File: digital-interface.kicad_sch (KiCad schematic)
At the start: 23 parts, among them U701 Si8641BD-B-IS2, U702 R05C05TE05S

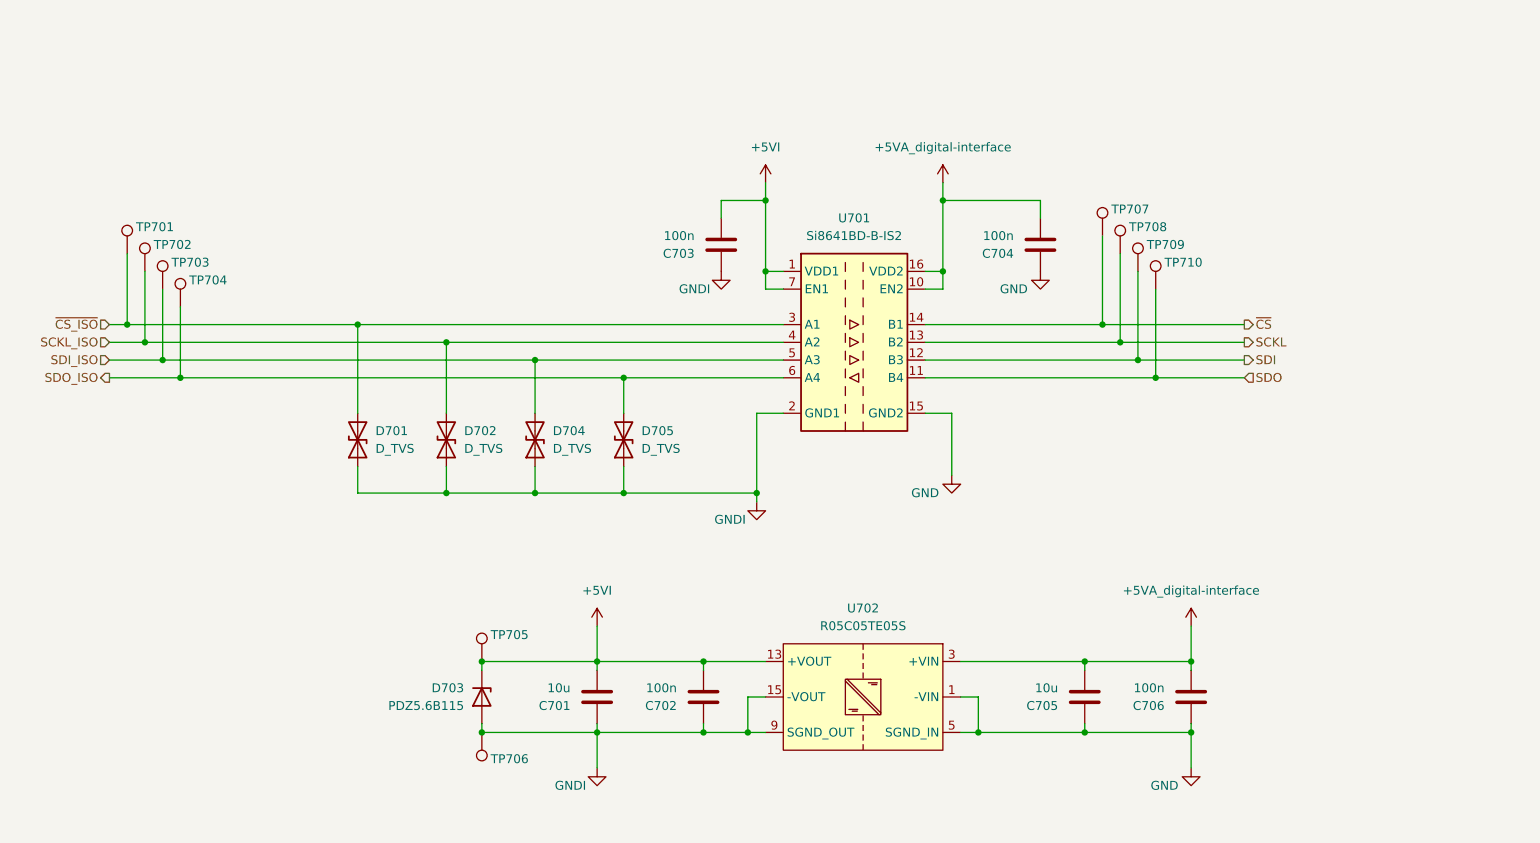
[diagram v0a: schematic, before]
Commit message: edit digital-interface rise time limitation with lowpass filter
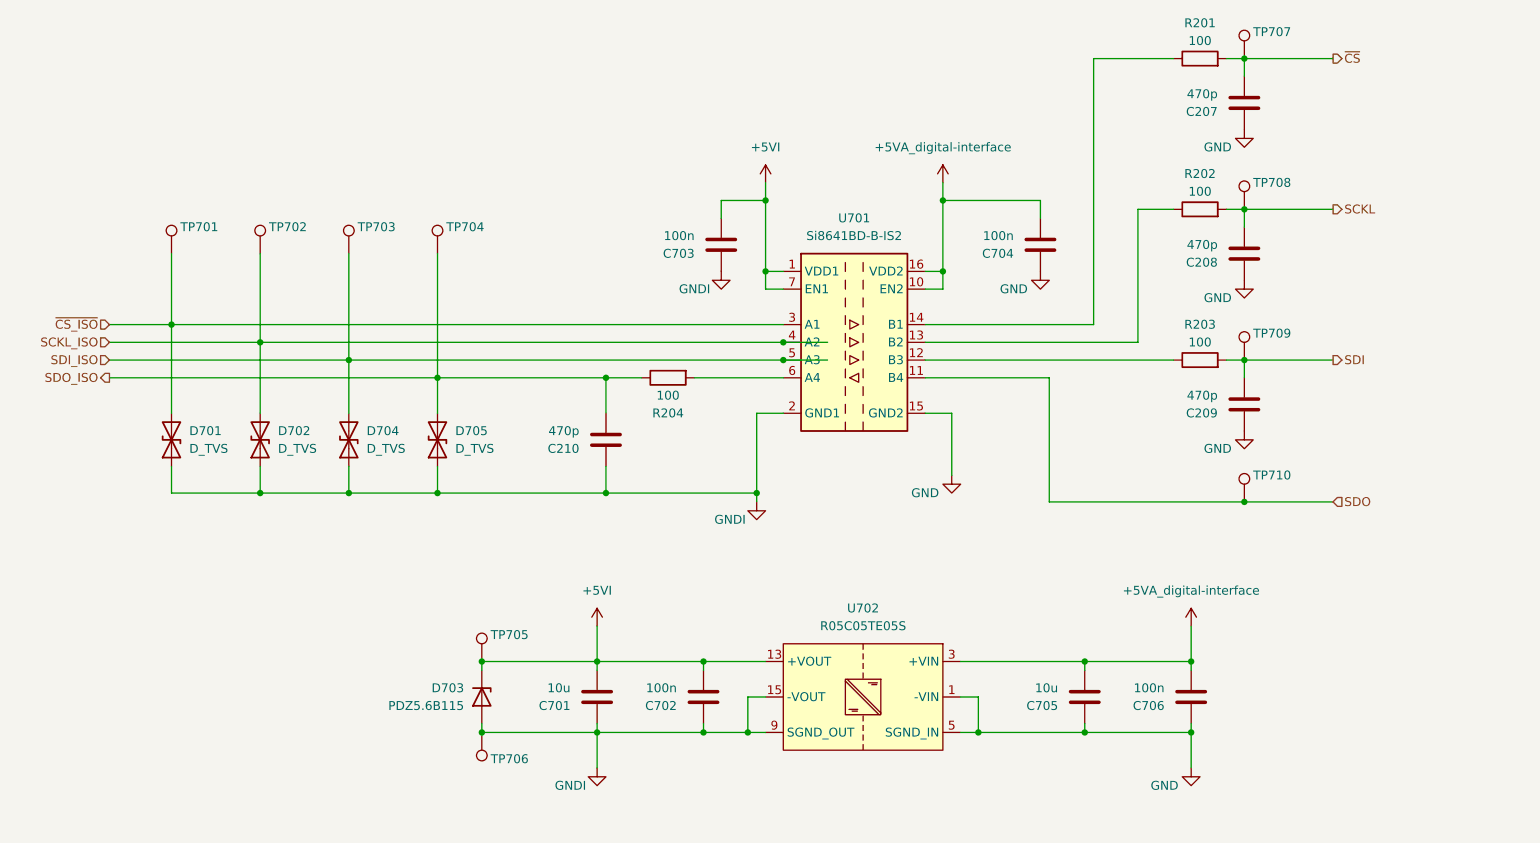
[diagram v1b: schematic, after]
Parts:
- added C207, C208, C209, C210: 470p, pss:C_0805_2012Metric_Pad1.18x1.45mm_HandSolder, symbol enclosure:C
- added R201, R202, R203, R204: 100, pss:R_1210_3225Metric_Pad1.30x2.65mm_HandSolder, symbol enclosure:R
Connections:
- net GND: now also C207.1, C208.1, C209.1
- net GNDI: now also C210.1
- net SCKL: now also C208.2, R202.2; no longer U701.13 (B2)
- net SDI: now also C209.2, R203.2; no longer U701.12 (B3)
- net SDO_ISO: now also C210.2, R204.1; no longer U701.6 (A4)
- net ~{CS}: now also C207.2, R201.2; no longer U701.14 (B1)
- new net: R204.2, U701.6 (A4)
- new net: R201.1, U701.14 (B1)
- new net: R202.1, U701.13 (B2)
- new net: R203.1, U701.12 (B3)
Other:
- moved on the sheet: D701, D702, D704, D705, TP701, TP702, TP703, TP704, TP707, TP708, TP709, TP710

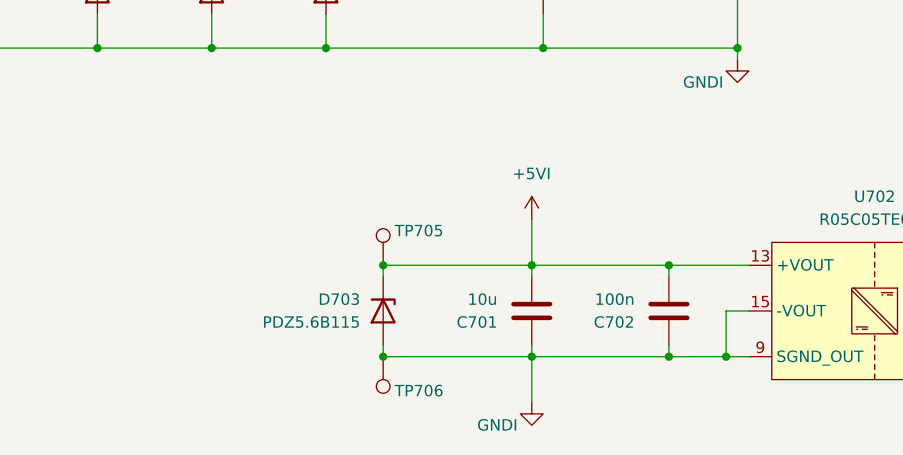
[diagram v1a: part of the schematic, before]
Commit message: edit enclosure digital-interface increase minimal load current to 15mA
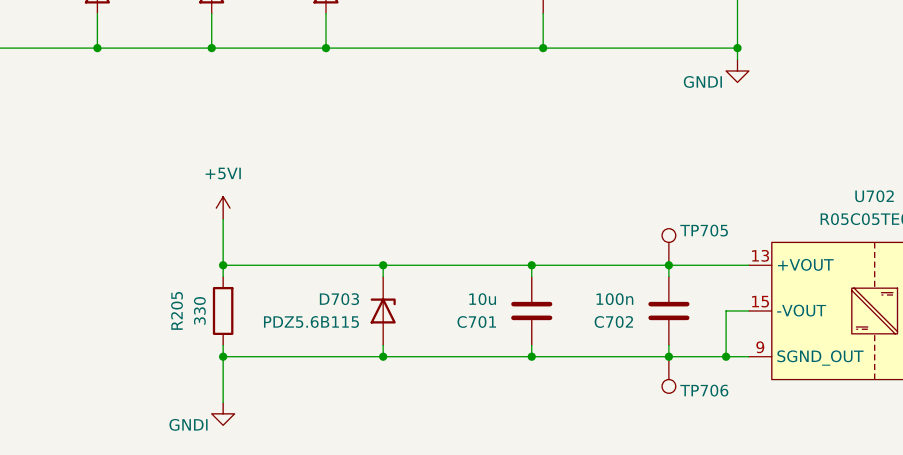
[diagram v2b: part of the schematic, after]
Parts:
- added R205: 330, pss:R_1210_3225Metric_Pad1.30x2.65mm_HandSolder, symbol enclosure:R
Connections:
- net +5VI: now also R205.2
- net GNDI: now also R205.1
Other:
- moved on the sheet: TP705, TP706
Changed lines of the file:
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@@
 	)
 	(junction
+		(at 76.2 116.84)
+		(diameter 0)
+		(color 0 0 0 0)
+	)
+	(junction
 		(at 160.02 50.8)
 		(diameter 0)
@@
 		(color 0 0 0 0)
 	)
-	(wire
-		(pts
-			(xy 110.49 116.84) (xy 110.49 111.76)
-		)
-		(stroke
-			(width 0)
-			(type default)
-		)
+	(junction
+		(at 76.2 127)
+		(diameter 0)
+		(color 0 0 0 0)
 	)
 	(wire
 		(pts
-			(xy 93.98 116.84) (xy 110.49 116.84)
+			(xy 76.2 116.84) (xy 76.2 111.76)
 		)
 		(stroke
@@
 	(wire
 		(pts
+			(xy 76.2 118.11) (xy 76.2 116.84)
+		)
+		(stroke
+			(width 0)
+			(type default)
+		)
+	)
+	(wire
+		(pts
 			(xy 110.49 125.73) (xy 110.49 127)
 		)
@@
 	(wire
 		(pts
+			(xy 93.98 127) (xy 76.2 127)
+		)
+		(stroke
+			(width 0)
+			(type default)
+		)
+	)
+	(wire
+		(pts
+			(xy 93.98 116.84) (xy 110.49 116.84)
+		)
+		(stroke
+			(width 0)
+			(type default)
+		)
+	)
+	(wire
+		(pts
 			(xy 125.73 125.73) (xy 125.73 127)
 		)
@@
 	(wire
 		(pts
-			(xy 110.49 127) (xy 110.49 132.08)
+			(xy 76.2 127) (xy 76.2 132.08)
 		)
 		(stroke
@@
 	(wire
 		(pts
-			(xy 110.49 127) (xy 125.73 127)
-		)
-		(stroke
-			(width 0)
-			(type default)
-		)
-	)
-	(wire
-		(pts
 			(xy 62.23 92.71) (xy 62.23 88.9)
 		)
@@
 	(wire
 		(pts
+			(xy 76.2 116.84) (xy 93.98 116.84)
+		)
+		(stroke
+			(width 0)
+			(type default)
+		)
+	)
+	(wire
+		(pts
 			(xy 181.61 30.48) (xy 193.04 30.48)
 		)
@@
 	(wire
 		(pts
+			(xy 125.73 127) (xy 110.49 127)
+		)
+		(stroke
+			(width 0)
+			(type default)
+		)
+	)
+	(wire
+		(pts
+			(xy 76.2 127) (xy 76.2 125.73)
+		)
+		(stroke
+			(width 0)
+			(type default)
+		)
+	)
+	(wire
+		(pts
 			(xy 203.2 73.66) (xy 200.66 73.66)
 		)
@@
 	(symbol
 		(lib_id "enclosure:+5VI")
-		(at 110.49 111.76 0)
+		(at 76.2 111.76 0)
 		(unit 1)
 		(exclude_from_sim no)
@@
 		(fields_autoplaced yes)
 		(property "Reference" "#PWR0701"
-			(at 110.49 115.57 0)
+			(at 76.2 115.57 0)
 			(effects
 				(font
@@
 		)
 		(property "Value" "+5VI"
-			(at 110.49 106.68 0)
+			(at 76.2 106.68 0)
 			(effects
 				(font
@@
 		)
 		(property "Footprint" ""
-			(at 110.49 111.76 0)
+			(at 76.2 111.76 0)
 			(effects
 				(font
@@
 		)
 		(property "Datasheet" ""
-			(at 110.49 111.76 0)
+			(at 76.2 111.76 0)
 			(effects
 				(font
@@
 		)
 		(property "Description" "Power symbol creates a global label with name \"+5VI\""
-			(at 110.49 111.76 0)
+			(at 76.2 111.76 0)
 			(effects
 				(font
@@
 	)
 	(symbol
+		(lib_id "enclosure:R")
+		(at 76.2 121.92 180)
+		(unit 1)
+		(exclude_from_sim no)
+		(in_bom yes)
+		(on_board yes)
+		(dnp no)
+		(property "Reference" "R205"
+			(at 71.12 121.92 90)
+			(effects
+				(font
+					(size 1.27 1.27)
+				)
+			)
+		)
+		(property "Value" "330"
+			(at 73.66 121.92 90)
+			(effects
+				(font
+					(size 1.27 1.27)
+				)
+			)
+		)
+		(property "Footprint" "pss:R_1210_3225Metric_Pad1.30x2.65mm_HandSolder"
+			(at 77.978 121.92 90)
+			(effects
+				(font
+					(size 1.27 1.27)
+				)
+				(hide yes)
+			)
+		)
+		(property "Datasheet" "./datasheet/R_SMD_Yageo.pdf"
+			(at 76.2 121.92 0)
+			(effects
+				(font
+					(size 1.27 1.27)
+				)
+				(hide yes)
+			)
+		)
+		(property "Description" "Resistor"
+			(at 76.2 121.92 0)
+			(effects
+				(font
+					(size 1.27 1.27)
+				)
+				(hide yes)
+			)
+		)
+		(property "MPN" "RC1210FR-07330RL"
+			(at 76.2 121.92 0)
+			(effects
+				(font
+					(size 1.27 1.27)
+				)
+				(hide yes)
+			)
+		)
+		(property "VPN" "603-RC1210FR-07330RL"
+			(at 76.2 121.92 0)
+			(effects
+				(font
+					(size 1.27 1.27)
+				)
+				(hide yes)
+			)
+		)
+		(pin "1"
+		)
+		(pin "2"
+		)
+		(instances
+			(project "enclosure"
+				(path "/8ec0899b-9d7b-491d-933a-49b74b34a0df/dc44c087-3b63-4db9-8fc8-89acb3b8154a"
+					(reference "R205")
+					(unit 1)
+				)
+			)
+		)
+	)
+	(symbol
 		(lib_id "enclosure:+5VI")
 		(at 134.62 48.26 0)
@@
 	(symbol
 		(lib_id "enclosure:GNDI")
-		(at 110.49 132.08 0)
+		(at 76.2 132.08 0)
 		(unit 1)
 		(exclude_from_sim no)
@@
 		(dnp no)
 		(property "Reference" "#PWR0702"
-			(at 110.49 138.43 0)
+			(at 76.2 138.43 0)
 			(effects
 				(font
@@
 		)
 		(property "Value" "GNDI"
-			(at 106.68 134.62 0)
+			(at 72.39 134.62 0)
 			(effects
 				(font
@@
 		)
 		(property "Footprint" ""
-			(at 110.49 132.08 0)
+			(at 76.2 132.08 0)
 			(effects
 				(font
@@
 		)
 		(property "Datasheet" ""
-			(at 110.49 132.08 0)
+			(at 76.2 132.08 0)
 			(effects
 				(font
@@
 		)
 		(property "Description" "Power symbol creates a global label with name \"GNDI\" , ground"
-			(at 110.49 132.08 0)
+			(at 76.2 132.08 0)
 			(effects
 				(font
@@
 	(symbol
 		(lib_id "enclosure:TestPoint")
-		(at 93.98 116.84 0)
+		(at 125.73 116.84 0)
 		(unit 1)
 		(exclude_from_sim no)
@@
 		(dnp no)
 		(property "Reference" "TP705"
-			(at 95.25 113.03 0)
+			(at 127 113.03 0)
 			(effects
 				(font
@@
 		)
 		(property "Value" "~"
-			(at 96.52 114.8079 0)
+			(at 128.27 114.8079 0)
 			(effects
 				(font
@@
 		)
 		(property "Footprint" "pss:TP_0805_2012Metric"
-			(at 99.06 116.84 0)
+			(at 130.81 116.84 0)
 			(effects
 				(font
@@
 		)
 		(property "Datasheet" "./datasheet/RCTCTE.pdf"
-			(at 99.06 116.84 0)
+			(at 130.81 116.84 0)
 			(effects
 				(font
@@
 		)
 		(property "Description" "test point"
-			(at 93.98 116.84 0)
+			(at 125.73 116.84 0)
 			(effects
 				(font
@@
 		)
 		(property "MPN" "RCTCTE"
-			(at 93.98 116.84 0)
+			(at 125.73 116.84 0)
 			(effects
 				(font
@@
 		)
 		(property "VPN" "660-RCTCTE"
-			(at 93.98 116.84 0)
+			(at 125.73 116.84 0)
 			(effects
 				(font
@@
 	(symbol
 		(lib_id "enclosure:TestPoint")
-		(at 93.98 127 0)
+		(at 125.73 127 0)
 		(mirror x)
 		(unit 1)
@@
 		(dnp no)
 		(property "Reference" "TP706"
-			(at 95.25 130.81 0)
+			(at 127 130.81 0)
 			(effects
 				(font
@@
 		)
 		(property "Value" "~"
-			(at 96.52 129.0321 0)
+			(at 128.27 129.0321 0)
 			(effects
 				(font
@@
 		)
 		(property "Footprint" "pss:TP_0805_2012Metric"
-			(at 99.06 127 0)
+			(at 130.81 127 0)
 			(effects
 				(font
@@
 		)
 		(property "Datasheet" "./datasheet/RCTCTE.pdf"
-			(at 99.06 127 0)
+			(at 130.81 127 0)
 			(effects
 				(font
@@
 		)
 		(property "Description" "test point"
-			(at 93.98 127 0)
+			(at 125.73 127 0)
 			(effects
 				(font
@@
 		)
 		(property "MPN" "RCTCTE"
-			(at 93.98 127 0)
+			(at 125.73 127 0)
 			(effects
 				(font
@@
 		)
 		(property "VPN" "660-RCTCTE"
-			(at 93.98 127 0)
+			(at 125.73 127 0)
 			(effects
 				(font

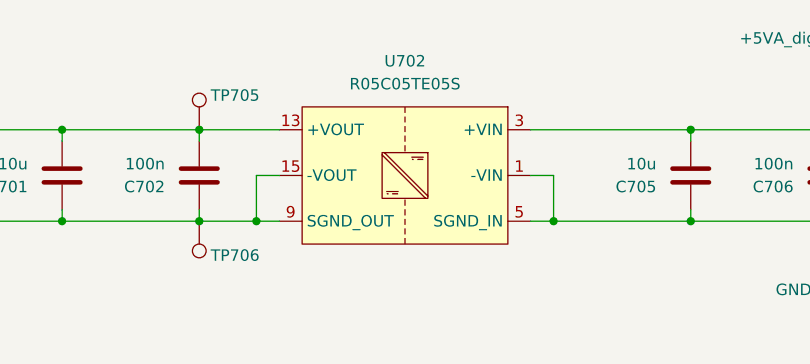
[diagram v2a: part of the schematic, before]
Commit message: edit enclosure digital-interface add esd protection resistor
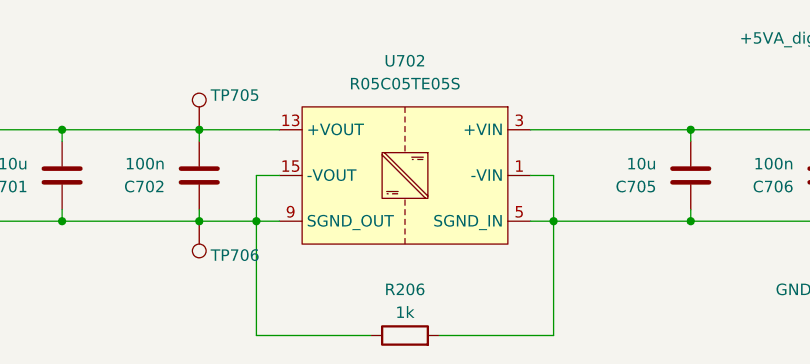
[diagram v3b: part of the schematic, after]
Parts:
- added R206: 1k, pss:R_1210_3225Metric_Pad1.30x2.65mm_HandSolder, symbol enclosure:R
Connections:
- net GND: now also R206.2
- net GNDI: now also R206.1
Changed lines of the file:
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@@
+	(wire
+		(pts
+			(xy 152.4 139.7) (xy 165.1 139.7)
+		)
+		(stroke
+			(width 0)
+			(type default)
+		)
+	)
 	(wire
 		(pts
@@
 	(wire
 		(pts
+			(xy 132.08 139.7) (xy 144.78 139.7)
+		)
+		(stroke
+			(width 0)
+			(type default)
+		)
+	)
+	(wire
+		(pts
 			(xy 195.58 111.76) (xy 195.58 116.84)
 		)
@@
 		(pts
 			(xy 133.35 81.28) (xy 137.16 81.28)
+		)
+		(stroke
+			(width 0)
+			(type default)
+		)
+	)
+	(wire
+		(pts
+			(xy 165.1 139.7) (xy 165.1 127)
+		)
+		(stroke
+			(width 0)
+			(type default)
+		)
+	)
+	(wire
+		(pts
+			(xy 132.08 127) (xy 132.08 139.7)
 		)
 		(stroke
@@
 					(unit 1)
 				)
+			)
+		)
+	)
+	(symbol
+		(lib_id "enclosure:R")
+		(at 148.59 139.7 90)
+		(unit 1)
+		(exclude_from_sim no)
+		(in_bom yes)
+		(on_board yes)
+		(dnp no)
+		(property "Reference" "R206"
+			(at 148.59 134.62 90)
+			(effects
+				(font
+					(size 1.27 1.27)
+				)
+			)
+		)
+		(property "Value" "1k"
+			(at 148.59 137.16 90)
+			(effects
+				(font
+					(size 1.27 1.27)
+				)
+			)
+		)
+		(property "Footprint" "pss:R_1210_3225Metric_Pad1.30x2.65mm_HandSolder"
+			(at 148.59 141.478 90)
+			(effects
+				(font
+					(size 1.27 1.27)
+				)
+				(hide yes)
+			)
+		)
+		(property "Datasheet" "./datasheet/R_SMD_Yageo.pdf"
+			(at 148.59 139.7 0)
+			(effects
+				(font
+					(size 1.27 1.27)
+				)
+				(hide yes)
+			)
+		)
+		(property "Description" "Resistor"
+			(at 148.59 139.7 0)
+			(effects
+				(font
+					(size 1.27 1.27)
+				)
+				(hide yes)
+			)
+		)
+		(property "MPN" "RC1210FR-071KL"
+			(at 148.59 139.7 0)
+			(effects
+				(font
+					(size 1.27 1.27)
+				)
+				(hide yes)
+			)
+		)
+		(property "VPN" "603-RC1210FR-071KL"
+			(at 148.59 139.7 0)
+			(effects
+				(font
+					(size 1.27 1.27)
+				)
+				(hide yes)
+			)
+		)
+		(pin "1"
+		)
+		(pin "2"
+		)
+		(instances
+			(project "enclosure"
+				(path "/8ec0899b-9d7b-491d-933a-49b74b34a0df/dc44c087-3b63-4db9-8fc8-89acb3b8154a"
+					(reference "R206")
+					(unit 1)
+				)
